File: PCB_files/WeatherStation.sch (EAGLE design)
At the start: 83 parts, among them CN1 S2B-PH-SM4, J1_RAIN RJ11, J2_WIND RJ11, Q1 SI2333DDS, Q2 BSS138, Q3 SI2333DDS, Q4 NC/SI2333DDS, Q5 BSS138, Q6 BSS138, Q7 NC/SI2333DDS, Q8 NC/BSS138, Q9 NC/SI2333DDS, U1 INA219BIDCNT, U3 SN74AUP2G14DCKR

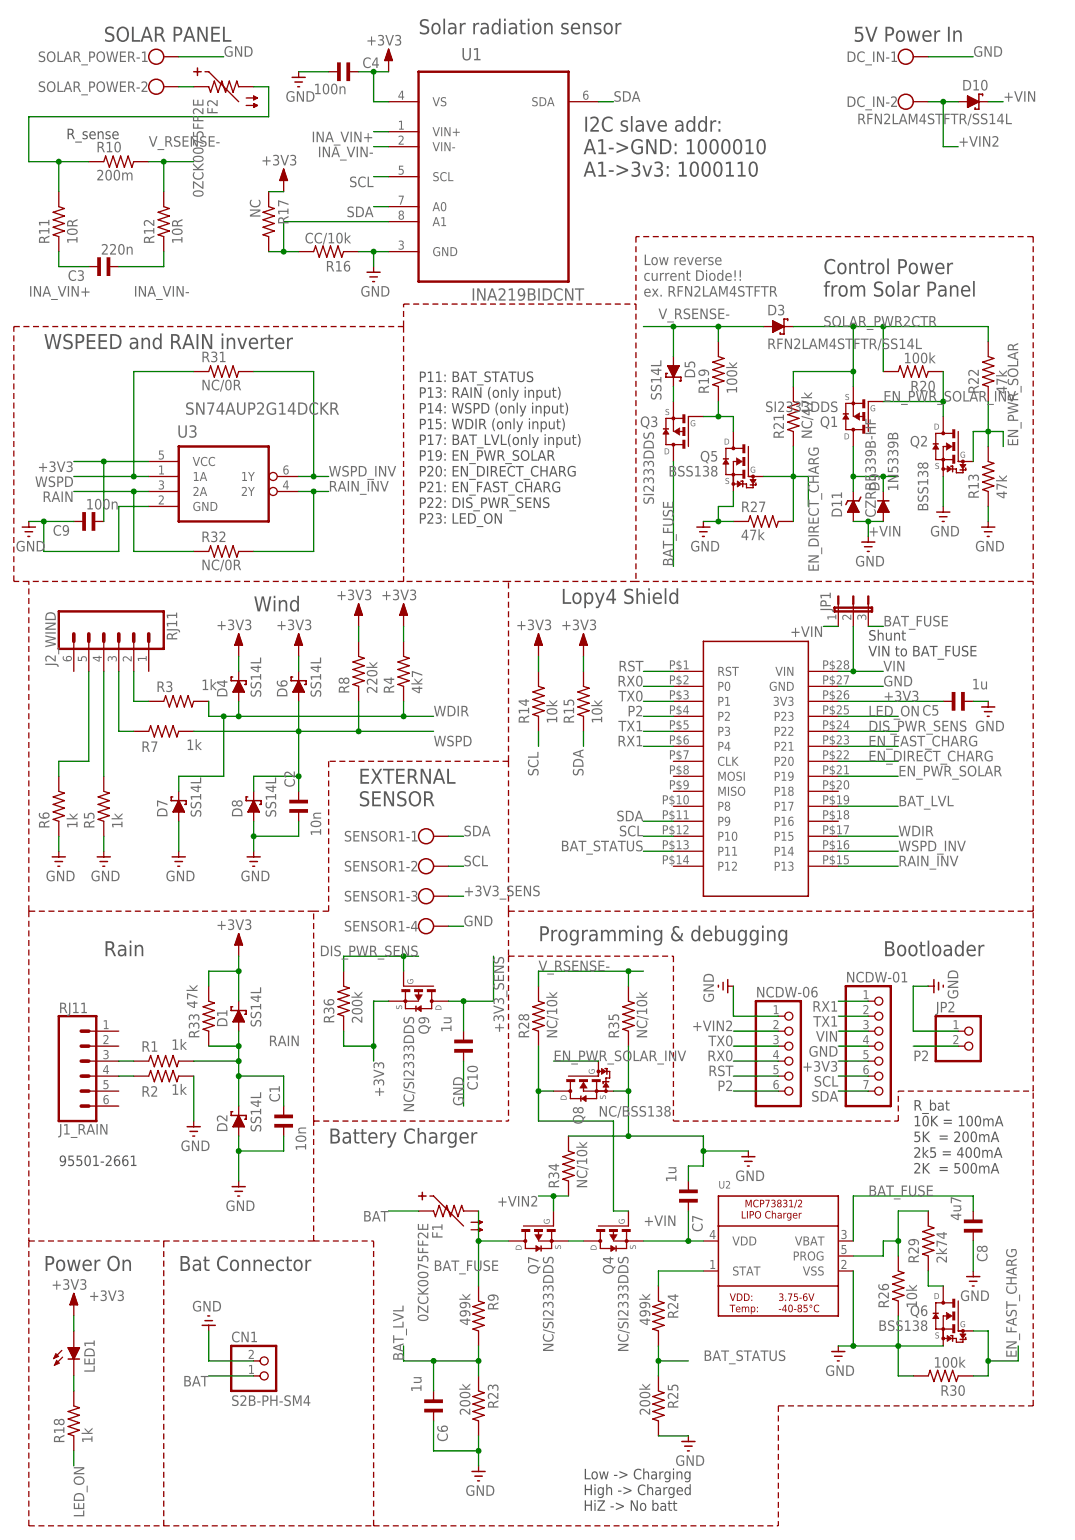
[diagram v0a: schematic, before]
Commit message: Update the repository structure;  Update BOM list; Add/update assembly files; Add link in readme file
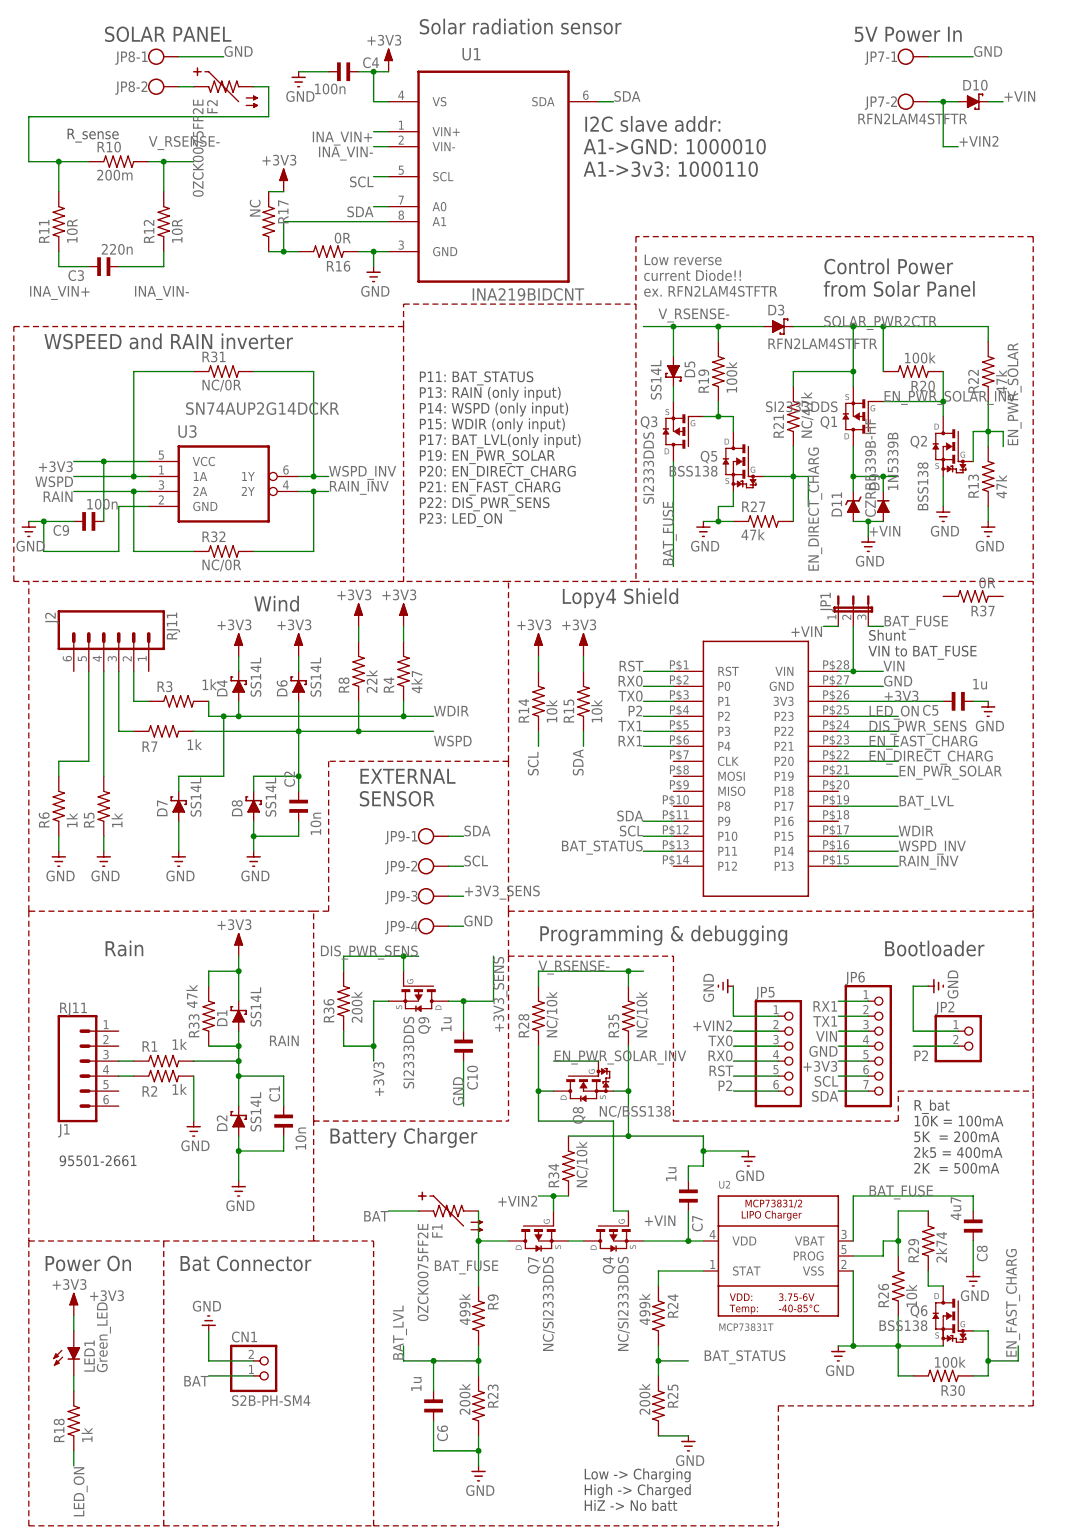
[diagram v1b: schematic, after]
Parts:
- added R37: 0R, rcl_imp:R-EU_R0603
- D10, D3: value RFN2LAM4STFTR/SS14L -> RFN2LAM4STFTR
- LED1: value (none) -> Green_LED
- Q9: value NC/SI2333DDS -> SI2333DDS
- R16: value CC/10k -> 0R
- R8: value 220k -> 22k
- U2: value (none) -> MCP73831T
- renumbered DC_IN to JP7, J1_RAIN to J1, J2_WIND to J2, NCDW-01 to JP6, NCDW-06 to JP5, SENSOR1 to JP9, SOLAR_POWER to JP8

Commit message: Updated Weather Station files
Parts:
- added C11, C12, C13: 100n, rcl_imp:C-EUC0603
- added D12: SS14L, diode:SCHOTTKY-DIODESUB_SMA_PROTO
- added J3: XMEGA-PDI, atmel-xmega_imp:XMEGA-PDI-3_FABIO
- added R38, R39: 10k, rcl_imp:R-EU_R0603
- added R40: 0R, rcl_imp:R-EU_R0603
- added U$3: ATXMEGAE5, atmel-xmega_imp:ATXMEGAE5-AU_SLIM_AU
- CN1: device adafruit_edit:JST_2PIN-SMT-RA -> adafruit:JST_2PINHOR_VER
- F2: device ptc-ntc:PTC-0805 -> ptc-ntc:PTC-0603_0805_PROTO_SLIM
- JP6: device pinhead:PINHD-1X7 -> pinhead:PINHD-1X8
- R26, R30, R31, R32, R4, R8: device rcl_imp:R-EU_R0603/R0805_PROTO_SLIM -> rcl_imp:R-EU_R0603
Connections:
- removed net WSPD_INV: R31.2, U$2.P14, U3.1Y
- new net N$14: R40.2, U3.1Y
- new net UART_!SS: JP6.1, U$3.(!SS!)PC4
- new net WD_!RST: J3.3, R38.2, U$3.!RESET!
- new net WD_PDI: J3.2, U$3.PDI
- new net WSPD_INV_: C13.1, R31.2, R40.1
- new net WSPD_INV_PULSE: C13.2, D12.C, R39.1, U$2.P14, U$3.(RXD0/MISO)PC6
- net +3V3: now also C11.2, C12.2, JP6.6, R38.1, U$3.AVCC@32, U$3.VCC@17; no longer JP6.5
- net BAT_FUSE: now also R37.2
- net GND: now also C11.1, C12.1, D12.A, J3.1, JP6.5, R39.2, U$3.GND@1, U$3.GND@18; no longer JP6.4
- net RAIN_INV: now also U$3.(TXD0/MOSI)PC7
- net RST: now also U$3.(XCK0/SCK)PC5
- net RX1: now also JP6.2, U$3.(TXD0)PC3; no longer JP6.1
- net SCL: now also JP6.7, U$3.(XCK0/SCL)PC1; no longer JP6.6
- net SDA: now also JP6.8, U$3.(SDA)PC0; no longer JP6.7
- net TX1: now also JP6.3, U$3.(RXD0)PC2; no longer JP6.2
- net VIN: now also JP6.4, R37.1; no longer JP6.3
- net WDIR: now also U$3.(ADC1)PA1
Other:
- note added: "-> WD_RESET_LOPY"
- note added: "-> WD_clear_counter"
- note added: "External WDT"
